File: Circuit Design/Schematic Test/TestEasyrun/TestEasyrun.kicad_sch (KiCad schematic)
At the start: 28 parts, among them U1 ESP32-WROOM-32

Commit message: Change the global labels
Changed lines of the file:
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@@
   (no_connect (at 116.84 73.66))
   (no_connect (at 116.84 83.82))
+  (wire (pts (xy 72.39 38.1) (xy 75.565 38.1))
+    (stroke (width 0) (type default) (color 0 0 0 0))
+  )
   (wire (pts (xy 50.8 36.83) (xy 50.8 40.005))
     (stroke (width 0) (type default) (color 0 0 0 0))
@@
     (stroke (width 0) (type default) (color 0 0 0 0))
   )
-  (wire (pts (xy 195.58 129.54) (xy 199.39 129.54))
-    (stroke (width 0) (type default) (color 0 0 0 0))
-  )
   (wire (pts (xy 45.085 77.47) (xy 39.37 77.47))
     (stroke (width 0) (type default) (color 0 0 0 0))
@@
     (stroke (width 0) (type default) (color 0 0 0 0))
   )
+  (wire (pts (xy 194.945 130.81) (xy 199.39 130.81))
+    (stroke (width 0) (type default) (color 0 0 0 0))
+  )
   (wire (pts (xy 34.29 22.86) (xy 39.37 22.86))
     (stroke (width 0) (type default) (color 0 0 0 0))
@@
     (stroke (width 0) (type default) (color 0 0 0 0))
   )
-  (wire (pts (xy 194.31 102.87) (xy 199.39 102.87))
-    (stroke (width 0) (type default) (color 0 0 0 0))
-  )
   (wire (pts (xy 196.85 114.3) (xy 199.39 114.3))
     (stroke (width 0) (type default) (color 0 0 0 0))
@@
     (stroke (width 0) (type default) (color 0 0 0 0))
   )
+  (wire (pts (xy 72.39 31.115) (xy 75.565 31.115))
+    (stroke (width 0) (type default) (color 0 0 0 0))
+  )
   (wire (pts (xy 240.03 113.03) (xy 240.03 115.57))
     (stroke (width 0) (type default) (color 0 0 0 0))
@@
     (stroke (width 0) (type default) (color 0 0 0 0))
   )
+  (wire (pts (xy 54.61 140.97) (xy 64.135 140.97))
+    (stroke (width 0) (type default) (color 0 0 0 0))
+  )
   (polyline (pts (xy 99.06 127) (xy 147.32 127))
     (stroke (width 0) (type default) (color 0 0 0 0))
   )
+  (wire (pts (xy 193.675 104.775) (xy 199.39 104.775))
+    (stroke (width 0) (type default) (color 0 0 0 0))
+  )
   (polyline (pts (xy 43.18 157.48) (xy 43.18 176.53))
     (stroke (width 0) (type default) (color 0 0 0 0))
@@
     (stroke (width 0) (type default) (color 0 0 0 0))
   )
-  (wire (pts (xy 57.15 123.19) (xy 54.61 123.19))
+  (wire (pts (xy 61.595 123.19) (xy 54.61 123.19))
     (stroke (width 0) (type default) (color 0 0 0 0))
   )
@@
     (stroke (width 0) (type default) (color 0 0 0 0))
   )
-  (wire (pts (xy 54.61 140.97) (xy 57.15 140.97))
-    (stroke (width 0) (type default) (color 0 0 0 0))
-  )
   (wire (pts (xy 196.85 111.76) (xy 199.39 111.76))
     (stroke (width 0) (type default) (color 0 0 0 0))
@@
     (stroke (width 0) (type default) (color 0 0 0 0))
   )
-  (wire (pts (xy 194.31 154.94) (xy 199.39 154.94))
-    (stroke (width 0) (type default) (color 0 0 0 0))
-  )
   (wire (pts (xy 148.59 53.34) (xy 149.225 53.34))
     (stroke (width 0) (type default) (color 0 0 0 0))
@@
     (stroke (width 0) (type default) (color 0 0 0 0))
   )
+  (wire (pts (xy 199.39 129.54) (xy 199.39 130.81))
+    (stroke (width 0) (type default) (color 0 0 0 0))
+  )
+  (wire (pts (xy 199.39 102.87) (xy 199.39 104.775))
+    (stroke (width 0) (type default) (color 0 0 0 0))
+  )
   (wire (pts (xy 148.59 96.52) (xy 149.225 96.52))
     (stroke (width 0) (type default) (color 0 0 0 0))
@@
     (stroke (width 0) (type default) (color 0 0 0 0))
   )
+  (wire (pts (xy 193.04 156.845) (xy 199.39 156.845))
+    (stroke (width 0) (type default) (color 0 0 0 0))
+  )
   (wire (pts (xy 148.59 73.66) (xy 149.225 73.66))
     (stroke (width 0) (type default) (color 0 0 0 0))
@@
     (stroke (width 0) (type default) (color 0 0 0 0))
   )
+  (wire (pts (xy 64.135 140.97) (xy 64.135 141.605))
+    (stroke (width 0) (type default) (color 0 0 0 0))
+  )
   (wire (pts (xy 132.08 151.13) (xy 132.08 153.67))
     (stroke (width 0) (type default) (color 0 0 0 0))
@@
   )
   (wire (pts (xy 54.61 125.73) (xy 57.15 125.73))
+    (stroke (width 0) (type default) (color 0 0 0 0))
+  )
+  (wire (pts (xy 199.39 154.94) (xy 199.39 156.845))
     (stroke (width 0) (type default) (color 0 0 0 0))
   )
@@
     (effects (font (size 1.27 1.27)) (justify left bottom))
   )
+  (label "3v3" (at 193.675 104.775 180)
+    (effects (font (size 1.27 1.27)) (justify right bottom))
+  )
+  (label "3v3" (at 57.15 143.51 0)
+    (effects (font (size 1.27 1.27)) (justify left bottom))
+  )
+  (label "3v3" (at 194.945 130.81 180)
+    (effects (font (size 1.27 1.27)) (justify right bottom))
+  )
+  (label "3v3" (at 106.68 166.37 180)
+    (effects (font (size 1.27 1.27)) (justify right bottom))
+  )
+  (label "3v3" (at 106.68 139.7 180)
+    (effects (font (size 1.27 1.27)) (justify right bottom))
+  )
+  (label "3v3" (at 193.04 156.845 180)
+    (effects (font (size 1.27 1.27)) (justify right bottom))
+  )
+  (label "3v3" (at 134.62 19.05 0)
+    (effects (font (size 1.27 1.27)) (justify left bottom))
+  )
+  (label "5v0" (at 52.07 162.56 180)
+    (effects (font (size 1.27 1.27)) (justify right bottom))
+  )
+  (label "3v3" (at 52.07 165.1 180)
+    (effects (font (size 1.27 1.27)) (justify right bottom))
+  )
+  (label "3v3" (at 75.565 38.1 0)
+    (effects (font (size 1.27 1.27)) (justify left bottom))
+  )
+  (label "3v3" (at 57.15 125.73 0)
+    (effects (font (size 1.27 1.27)) (justify left bottom))
+  )
+  (label "5v0" (at 75.565 31.115 0)
+    (effects (font (size 1.27 1.27)) (justify left bottom))
+  )
   (global_label "D{slash}C" (shape output) (at 154.94 101.6 0) (fields_autoplaced)
     (effects (font (size 1.27 1.27)) (justify left))
@@
     )
   )
-  (global_label "GND" (shape input) (at 57.15 140.97 0) (fields_autoplaced)
-    (effects (font (size 1.27 1.27)) (justify left))
-    (property "Intersheet References" "${INTERSHEET_REFS}" (id 0) (at 63.4336 140.8906 0)
-      (effects (font (size 1.27 1.27)) (justify right) hide)
-    )
-  )
   (global_label "Butt_No_D" (shape input) (at 132.08 139.7 0) (fields_autoplaced)
     (effects (font (size 1.27 1.27)) (justify left))
@@
     )
   )
-  (global_label "MISO" (shape input) (at 57.15 123.19 0) (fields_autoplaced)
-    (effects (font (size 1.27 1.27)) (justify left))
-    (property "Intersheet References" "${INTERSHEET_REFS}" (id 0) (at 64.0704 123.1106 0)
-      (effects (font (size 1.27 1.27)) (justify left) hide)
-    )
-  )
-  (hierarchical_label "3v3" (shape input) (at 194.31 102.87 180)
-    (effects (font (size 1.27 1.27)) (justify right))
-  )
-  (hierarchical_label "5v0" (shape input) (at 52.07 162.56 180)
-    (effects (font (size 1.27 1.27)) (justify right))
-  )
-  (hierarchical_label "3v3" (shape input) (at 57.15 125.73 0)
-    (effects (font (size 1.27 1.27)) (justify left))
-  )
-  (hierarchical_label "3v3" (shape input) (at 57.15 143.51 0)
-    (effects (font (size 1.27 1.27)) (justify left))
-  )
-  (hierarchical_label "3v3" (shape input) (at 195.58 129.54 180)
-    (effects (font (size 1.27 1.27)) (justify right))
-  )
-  (hierarchical_label "3v3" (shape input) (at 106.68 166.37 180)
-    (effects (font (size 1.27 1.27)) (justify right))
+  (global_label "MISO" (shape input) (at 61.595 123.19 0) (fields_autoplaced)
+    (effects (font (size 1.27 1.27)) (justify left))
+    (property "Intersheet References" "${INTERSHEET_REFS}" (id 0) (at 68.5154 123.1106 0)
+      (effects (font (size 1.27 1.27)) (justify left) hide)
+    )
   )
   (hierarchical_label "5v0" (shape input) (at 245.11 91.44 180)
-    (effects (font (size 1.27 1.27)) (justify right))
-  )
-  (hierarchical_label "3v3" (shape input) (at 106.68 139.7 180)
-    (effects (font (size 1.27 1.27)) (justify right))
-  )
-  (hierarchical_label "3v3" (shape input) (at 194.31 154.94 180)
-    (effects (font (size 1.27 1.27)) (justify right))
-  )
-  (hierarchical_label "3v3" (shape input) (at 134.62 19.05 180)
-    (effects (font (size 1.27 1.27)) (justify right))
-  )
-  (hierarchical_label "3v3" (shape input) (at 52.07 165.1 180)
     (effects (font (size 1.27 1.27)) (justify right))
   )
@@
     (pin "1")
   )
+  (symbol (lib_id "power:GND") (at 64.135 141.605 0) (unit 1)
+    (in_bom yes) (on_board yes) (fields_autoplaced)
+    (property "Reference" "#PWR?" (id 0) (at 64.135 147.955 0)
+      (effects (font (size 1.27 1.27)) hide)
+    )
+    (property "Value" "GND" (id 1) (at 64.135 146.05 0))
+    (property "Footprint" "" (id 2) (at 64.135 141.605 0)
+      (effects (font (size 1.27 1.27)) hide)
+    )
+    (property "Datasheet" "" (id 3) (at 64.135 141.605 0)
+      (effects (font (size 1.27 1.27)) hide)
+    )
+    (pin "1")
+  )
   (symbol (lib_id "power:GND") (at 266.065 129.54 0) (unit 1)
     (in_bom yes) (on_board yes)
@@
       (reference "#PWR?") (unit 1) (value "GND") (footprint "")
     )
+    (path "/869d27ab-c976-4214-98ac-f180ecf47fb4"
+      (reference "#PWR?") (unit 1) (value "GND") (footprint "")
+    )
     (path "/ce33739c-5d28-4c4f-8ccf-84b467a2a283/88f4cff7-9710-4ace-a6dc-ce88ebe85e75"
       (reference "#PWR?") (unit 1) (value "GND") (footprint "")
@@
     )
     (path "/ce33739c-5d28-4c4f-8ccf-84b467a2a283/5ded5e05-91c3-4914-acd8-46f44022acc0/b4b31f94-7238-4ebb-8945-f8429e813474"
-      (reference "D_GREEN") (unit 1) (value "LED") (footprint "")
+      (reference "D_GREEN") (unit 1) (value "LED") (footprint "LED_SMD:LED_0805_2012Metric_Pad1.15x1.40mm_HandSolder")
     )
     (path "/ce33739c-5d28-4c4f-8ccf-84b467a2a283/5ded5e05-91c3-4914-acd8-46f44022acc0/61395088-d6a5-48f8-bf04-3d49b707028e"
-      (reference "D_RED") (unit 1) (value "LED") (footprint "")
+      (reference "D_RED") (unit 1) (value "LED") (footprint "LED_SMD:LED_0805_2012Metric_Pad1.15x1.40mm_HandSolder")
     )
     (path "/ce33739c-5d28-4c4f-8ccf-84b467a2a283/ba09b7a2-59f0-45b6-95a4-046331578e0c"

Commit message: Ready to merge
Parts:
- added C? (x2): C, Capacitor_SMD:C_0805_2012Metric_Pad1.18x1.45mm_HandSolder, symbol Device:C
- added R?: 220, Resistor_SMD:R_0805_2012Metric_Pad1.20x1.40mm_HandSolder, symbol Device:R
- R5: value 10K -> 220
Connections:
- net 3v3: now also C?.1, C?.1
- net Butt_D: now also C?.2
- net Butt_No_D: now also C?.2
- net at C1.1, R1.2, U1.3 (EN): now also R?.1; no longer ESP_Reset1.2
- new net: ESP_Reset1.2, R?.2
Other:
- moved on the sheet: C1, ESP_Reset1, R5

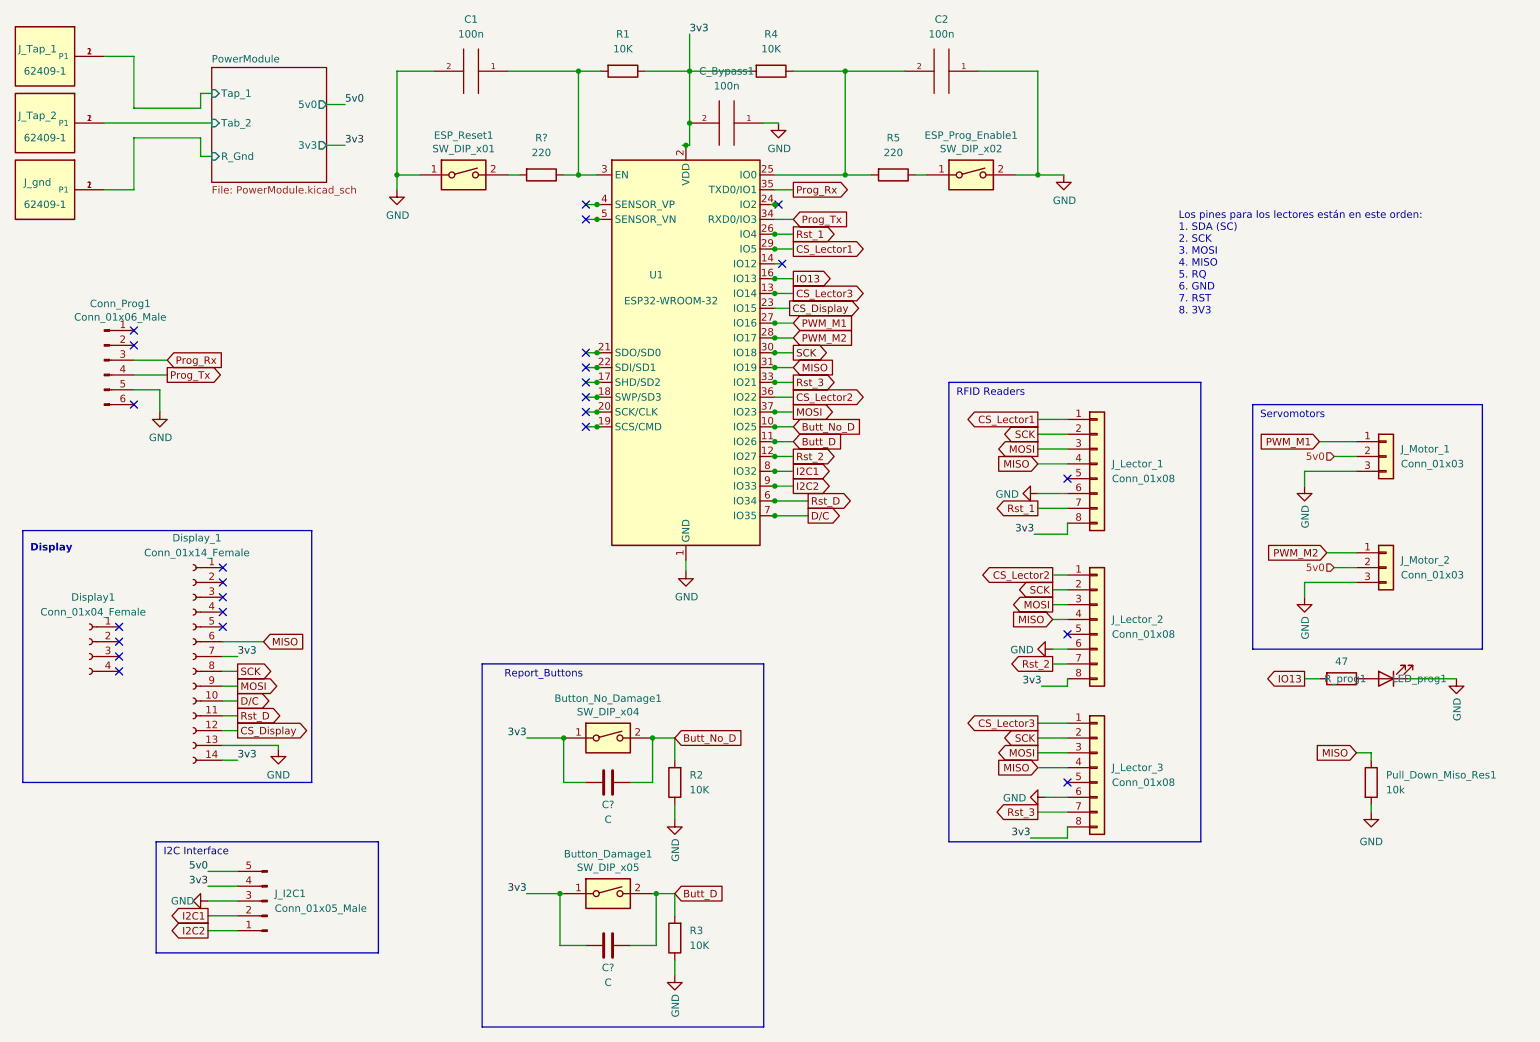
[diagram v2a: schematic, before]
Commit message: Add conection changes
Add conection changes, using different types of hierarchien
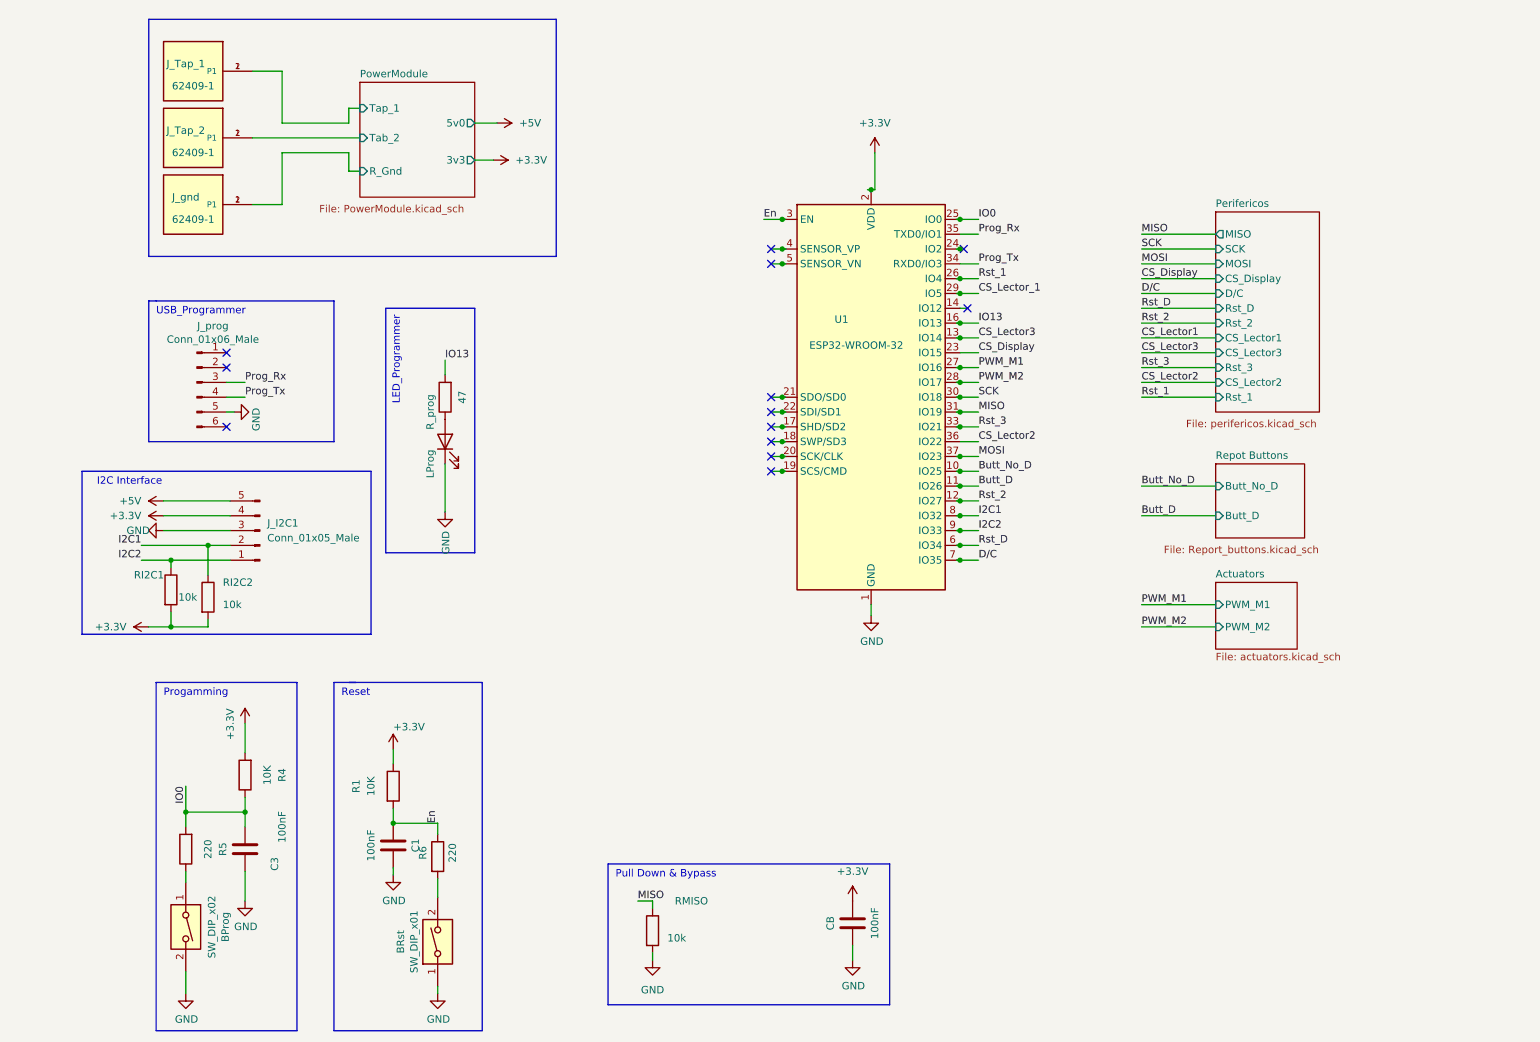
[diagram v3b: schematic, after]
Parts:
- removed Button_Damage1: SW_DIP_x05, symbol Switch:SW_DIP_x01
- removed Button_No_Damage1: SW_DIP_x04, symbol Switch:SW_DIP_x01
- removed C1, C2, C_Bypass1: 100n, Capacitor_SMD:C_0805_2012Metric_Pad1.18x1.45mm_HandSolder, symbol pspice:CAP
- removed C? (x2): C, Capacitor_SMD:C_0805_2012Metric_Pad1.18x1.45mm_HandSolder, symbol Device:C
- removed Display1: Conn_01x04_Female, Connector_PinSocket_2.54mm:PinSocket_1x04_P2.54mm_Vertical, symbol Connector:Conn_01x04_Female
- removed Display_1: Conn_01x14_Female, Connector_PinSocket_2.54mm:PinSocket_1x14_P2.54mm_Vertical, symbol Connector:Conn_01x14_Female
- removed J_Lector_1, J_Lector_2, J_Lector_3: Conn_01x08, Connector_PinHeader_2.54mm:PinHeader_1x08_P2.54mm_Vertical, symbol Connector_Generic:Conn_01x08
- removed J_Motor_1, J_Motor_2: Conn_01x03, Connector_PinHeader_2.54mm:PinHeader_1x03_P2.54mm_Vertical, symbol Connector_Generic:Conn_01x03
- removed R2, R3: 10K, Resistor_SMD:R_0805_2012Metric_Pad1.20x1.40mm_HandSolder, symbol Device:R
- added C1, C3, CB: 100nF, Capacitor_SMD:C_0805_2012Metric_Pad1.18x1.45mm_HandSolder, symbol Device:C
- added RI2C1, RI2C2: 10k, Resistor_SMD:R_0805_2012Metric_Pad1.20x1.40mm_HandSolder, symbol Device:R
- gave numbers to parts that had none: 1
- renumbered ESP_Prog_Enable1 to BProg, ESP_Reset1 to BRst, Conn_Prog1 to J_prog, LED_prog1 to LProg, Pull_Down_Miso_Res1 to RMISO, R_prog1 to R_prog
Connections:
- net CS_Lector1: no longer U1.29 (IO5)
- net GND: now also C1.1, C3.2, CB.2
- net I2C1: now also RI2C2.1
- net I2C2: now also RI2C1.1
- net IO0: now reaches R4.1, R5.2, U1.25 (IO0)
- net IO0: now also C3.1
- net En: now reaches R1.2, R6.1, U1.3 (EN)
- net En: now also C1.2
- net 3v3 renamed +3V3
- net +3V3: now also CB.1, RI2C1.2, RI2C2.2
- net 5v0 renamed +5V
- new net CS_Lector_1: U1.29 (IO5)
- no-connect marks 25 -> 13
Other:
- added sheet Actuators (actuators.kicad_sch)
- added sheet Perifericos (perifericos.kicad_sch)
- added sheet Repot Buttons (Report_buttons.kicad_sch)
- note added: "LED_Programmer"
- note added: "Progamming"
- note added: "Pull Down & Bypass"
- note added: "Reset"
- note added: "USB_Programmer"
- note removed: "Display"
- note removed: "Los pines para los lectores están en este orden: 1. SDA (SC) 2. SCK 3. MOSI 4. MISO 5. RQ 6. GND 7. RST 8. 3V3"
- note removed: "RFID Readers"
- note removed: "Report_Buttons"
- note removed: "Servomotors"
- moved on the sheet: BProg, BRst, J_I2C1, J_Tap_1, J_Tap_2, J_gnd, J_prog, LProg, R1, R4, R5, R6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
